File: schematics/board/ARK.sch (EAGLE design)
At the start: 205 parts, among them IC2 STM32F103C8T, Q5 8MHz

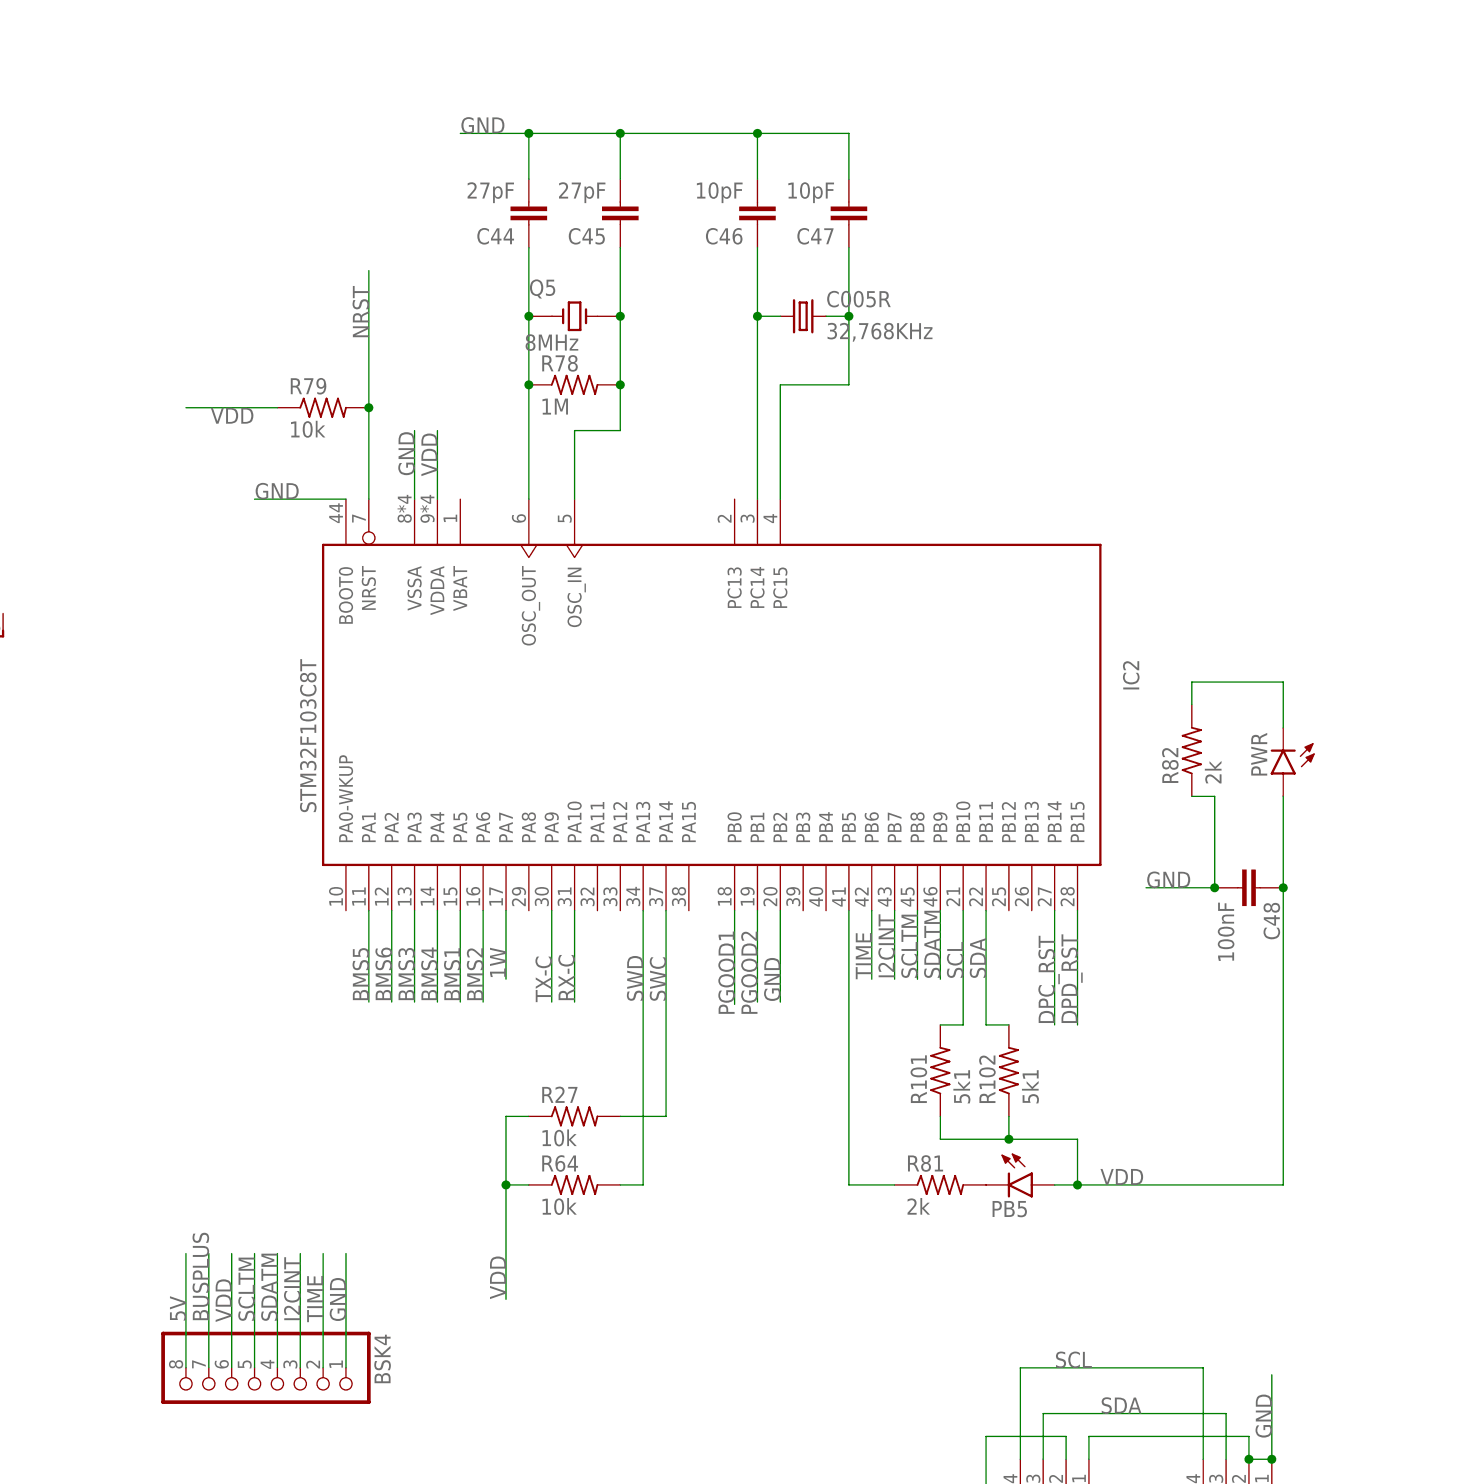
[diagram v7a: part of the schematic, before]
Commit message: Добавлены подтяжки i2c
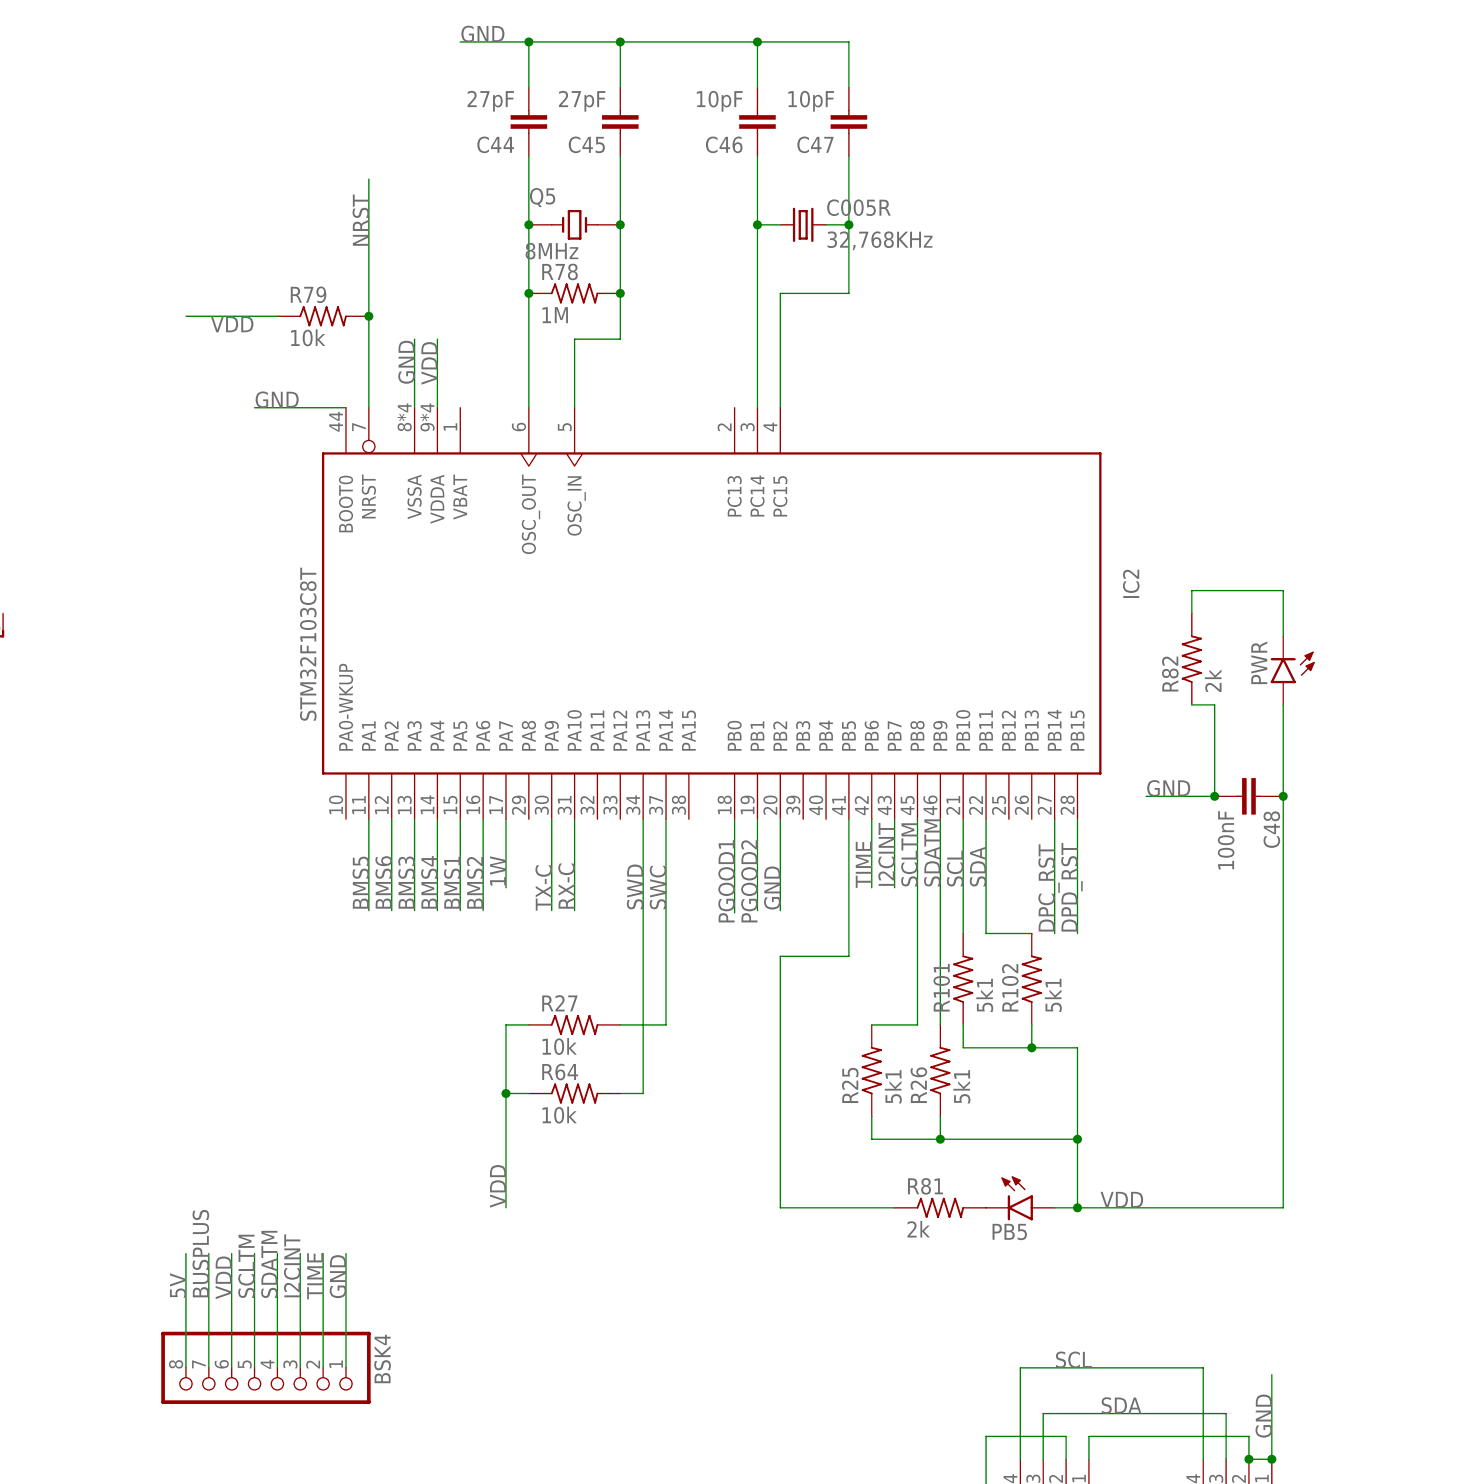
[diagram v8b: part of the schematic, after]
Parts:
- added R25, R26: 5k1, resistor:R-US_R0603
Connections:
- net SCLTM: now also R25.2
- net SDATM: now also R26.2
- net VDD: now also R25.1, R26.1
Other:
- moved on the sheet: C005R, C44, C45, C46, C47, C48, IC2, PB5, PWR, Q5, R101, R102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
